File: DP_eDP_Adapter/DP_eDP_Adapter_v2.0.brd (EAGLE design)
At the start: 50 x 50 mm, 61 parts, among them IC1 AP6502A, IC2 tiny2313, IC3 TLC5947XLP

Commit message: 
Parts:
- moved C29 5.73 mm to (7.30, -4.32), flipped to the bottom
- moved C25 5.61 mm to (8.70, -4.32), flipped to the bottom
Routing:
- net LANE3_P: track 26.7 -> 0.00 mm, vias 2 -> 0
- net LANE3_N: track 26.7 -> 0.00 mm, vias 2 -> 0
- net HPD: track 36.2 -> 30.2 mm
- net N$19_N: track 6.67 -> 9.04 mm
- net N$19_P: track 6.70 -> 9.00 mm

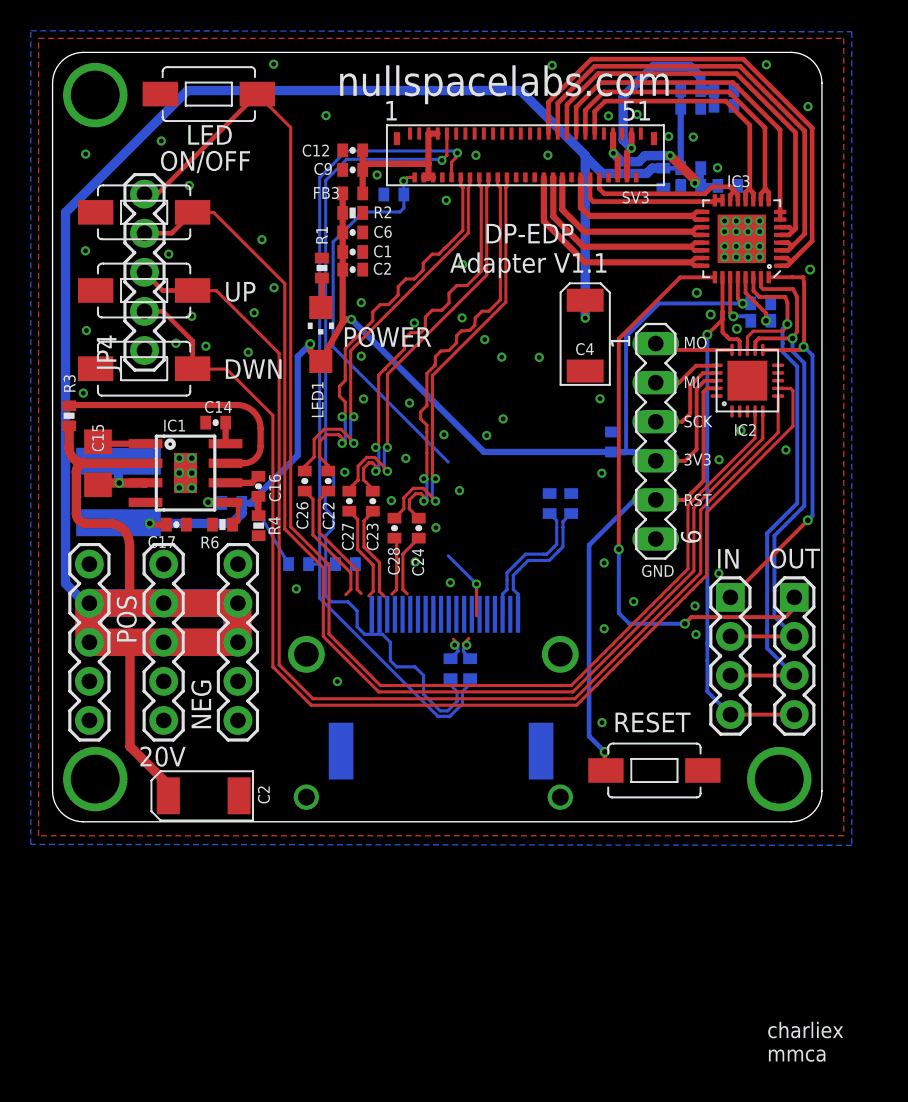
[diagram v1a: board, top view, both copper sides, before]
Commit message: 
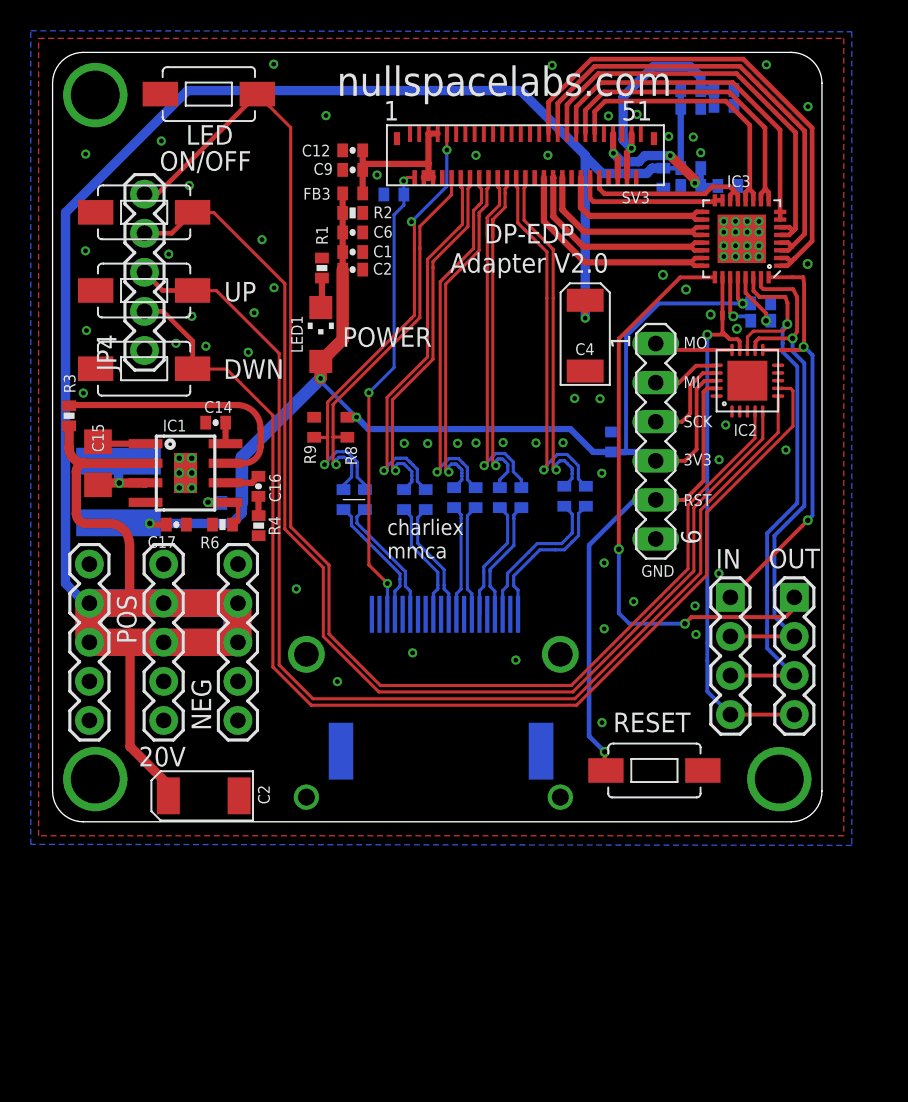
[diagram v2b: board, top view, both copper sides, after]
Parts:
- SV3: value DP_EDP_ADAPTER_EDP_CONNECTOR -> DP_EDP_ADAPTER_DP_EDP_ADAPTER_EDP_CONNECTOR; device DP_eDP_Adapter:DP_EDP_ADAPTER_EDP_MOLEX -> DP_eDP_Adapter_v2.0:DP_EDP_ADAPTER_DP_EDP_ADAPTER_EDP_MOLEX
- moved C20 13.7 mm to (-6.10, -4.06), turned to 270 degrees
- moved C21 12.3 mm to (-4.70, -4.06), turned to 270 degrees
- moved R8 9.44 mm to (-5.84, 0.64), flipped to the top, turned to 90 degrees
- moved R9 9.12 mm to (-8.00, 0.64), flipped to the top, turned to 270 degrees
- moved C28 7.13 mm to (4.06, -3.94), flipped to the bottom
- moved C24 6.96 mm to (5.46, -3.94), flipped to the bottom
- moved C27 6.81 mm to (1.09, -3.94), flipped to the bottom
- moved C23 6.68 mm to (2.49, -3.94), flipped to the bottom
- moved C26 6.56 mm to (-2.16, -4.06), flipped to the bottom
- moved C22 6.45 mm to (-0.75, -4.06), flipped to the bottom
- moved C29 1.06 mm to (8.26, -3.85)
- moved C25 1.06 mm to (9.65, -3.85)
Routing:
- net AUX_CH_N: track 54.3 -> 26.7 mm
- net LANE3_N: track 0.00 -> 24.7 mm, vias 0 -> 1
- net AUX_CH_P: track 54.3 -> 30.9 mm, vias 1 -> 3
- net LANE3_P: track 0.00 -> 23.4 mm, vias 0 -> 1
- net +3V3: track 93.3 -> 85.6 mm
- net AUX_P: track 2.05 -> 8.49 mm, vias 1 -> 0
- net AUX_N: track 2.09 -> 8.49 mm, vias 1 -> 0
- net LANE2_P: track 28.0 -> 23.8 mm, vias 2 -> 1
- net N$17_P: track 3.83 -> 7.90 mm
- net N$17_N: track 4.17 -> 7.90 mm
- net LANE1_P: track 27.0 -> 23.6 mm, vias 2 -> 1
- net LANE2_N: track 28.0 -> 25.1 mm, vias 2 -> 1
- net LANE1_N: track 27.0 -> 24.8 mm, vias 2 -> 1
- net LANE0_P: track 26.8 -> 24.7 mm, vias 2 -> 1
- net LANE0_N: track 26.9 -> 25.8 mm, vias 2 -> 1
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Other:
- board text added: "DP-EDP Adapter V2.0"
- board text removed: "DP-EDP Adapter V1.1"

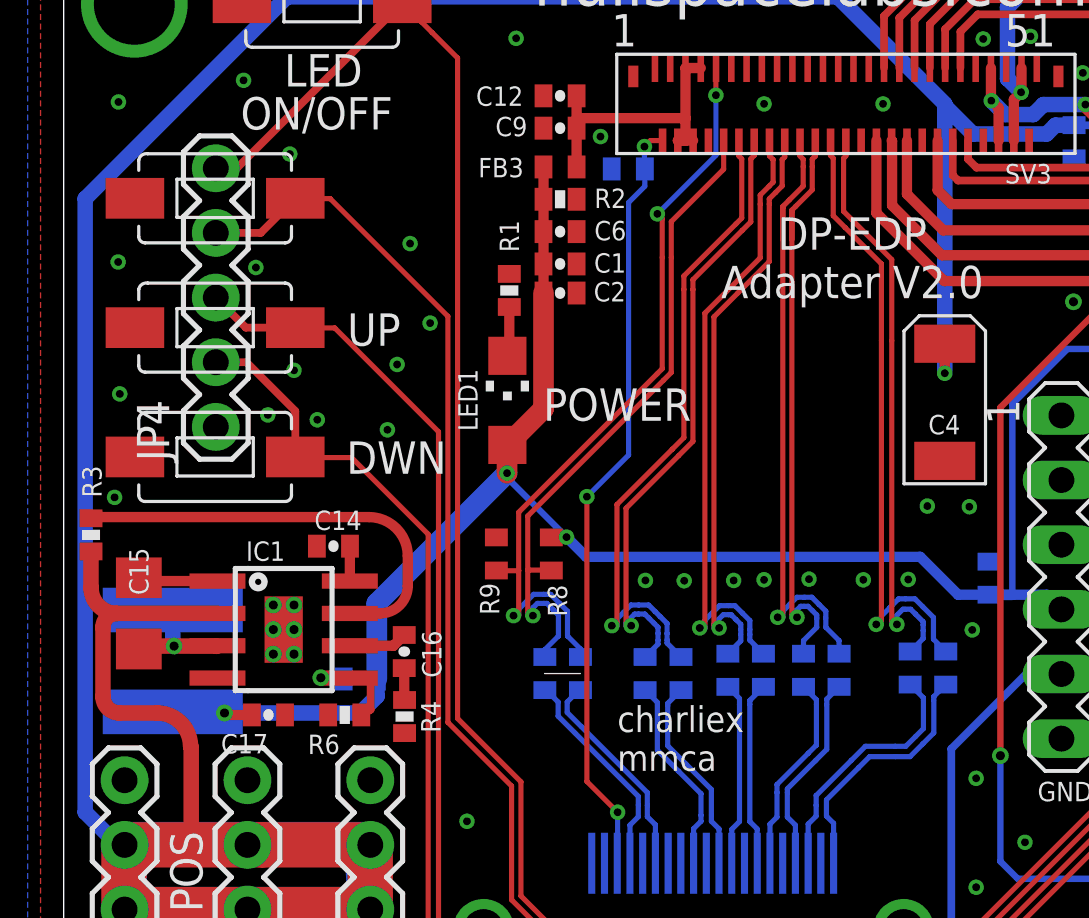
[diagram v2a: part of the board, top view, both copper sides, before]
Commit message: 
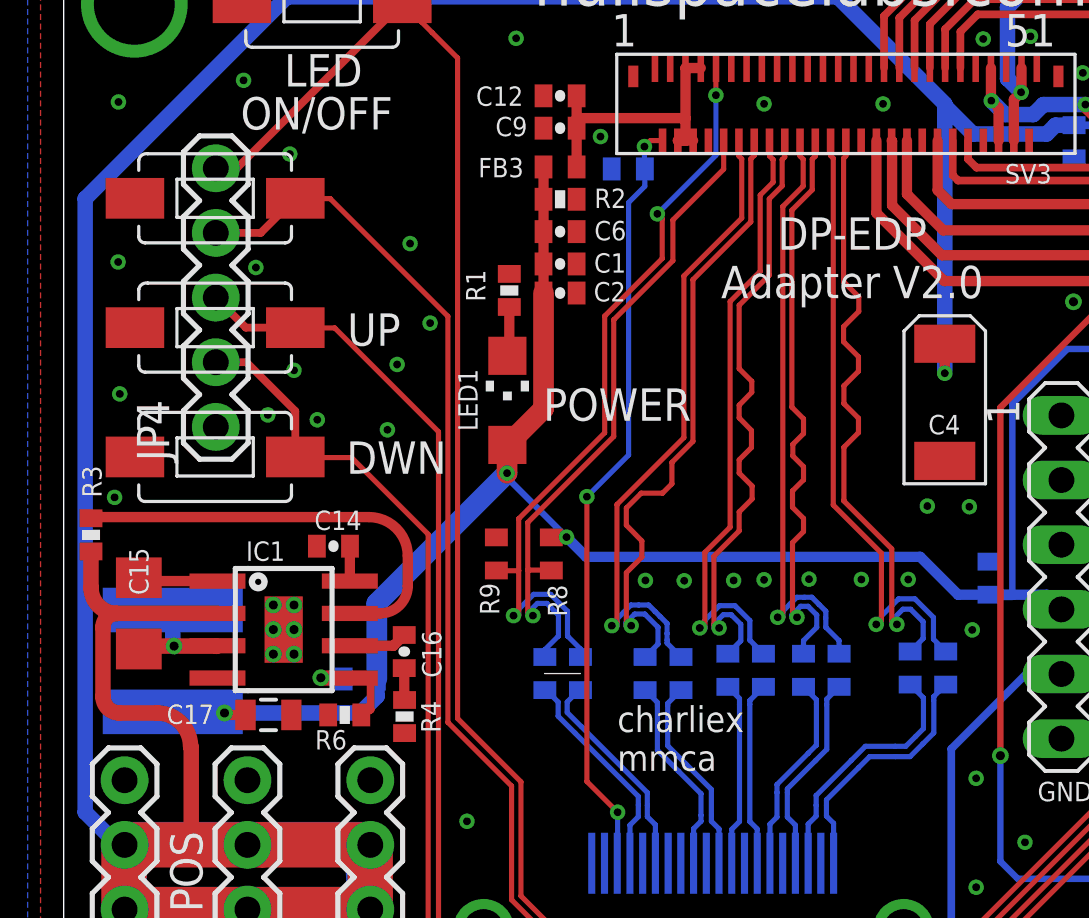
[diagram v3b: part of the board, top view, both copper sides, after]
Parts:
- C17: device SparkFun-Passives:0402-CAP -> SparkFun-Passives:0805
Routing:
- net LANE3_P: track 23.4 -> 24.8 mm
- net LANE2_N: track 25.1 -> 23.8 mm
- net LANE1_P: track 23.6 -> 24.8 mm
- net LANE0_P: track 24.7 -> 25.8 mm

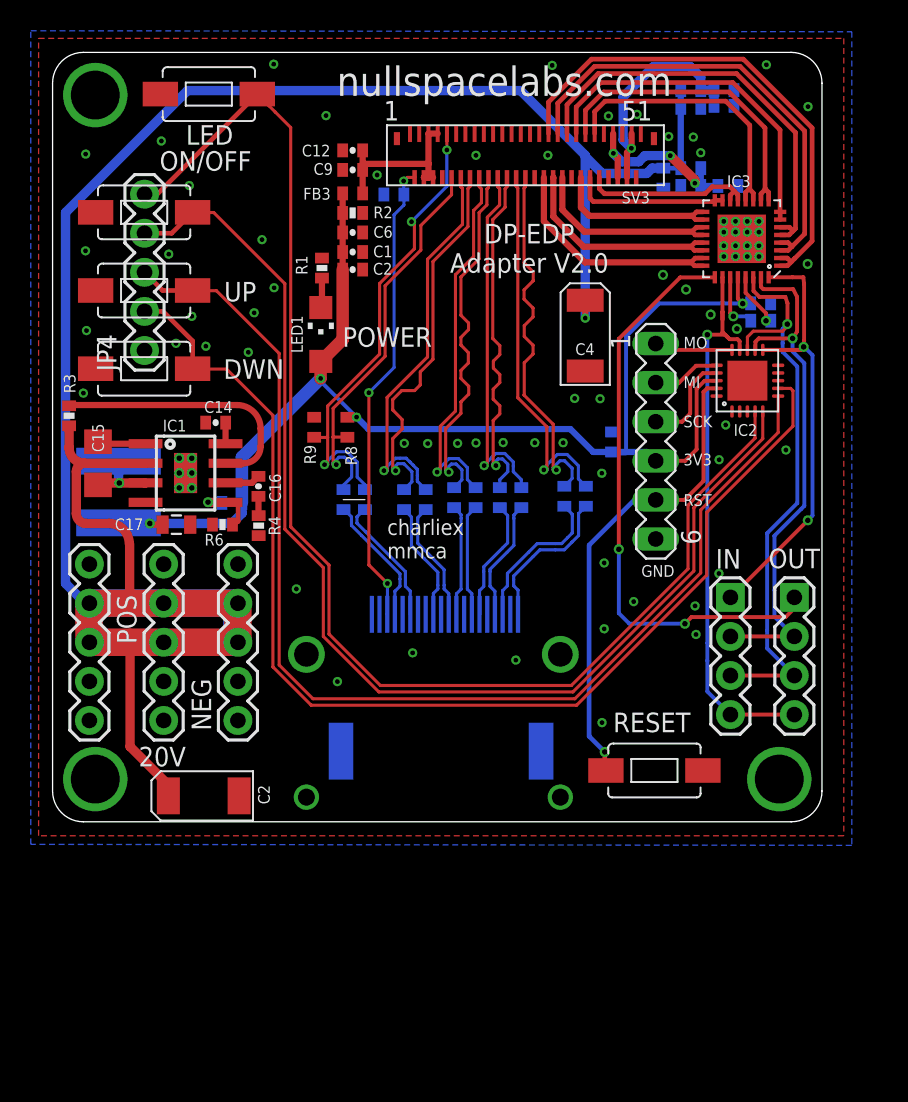
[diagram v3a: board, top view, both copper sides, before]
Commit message: 
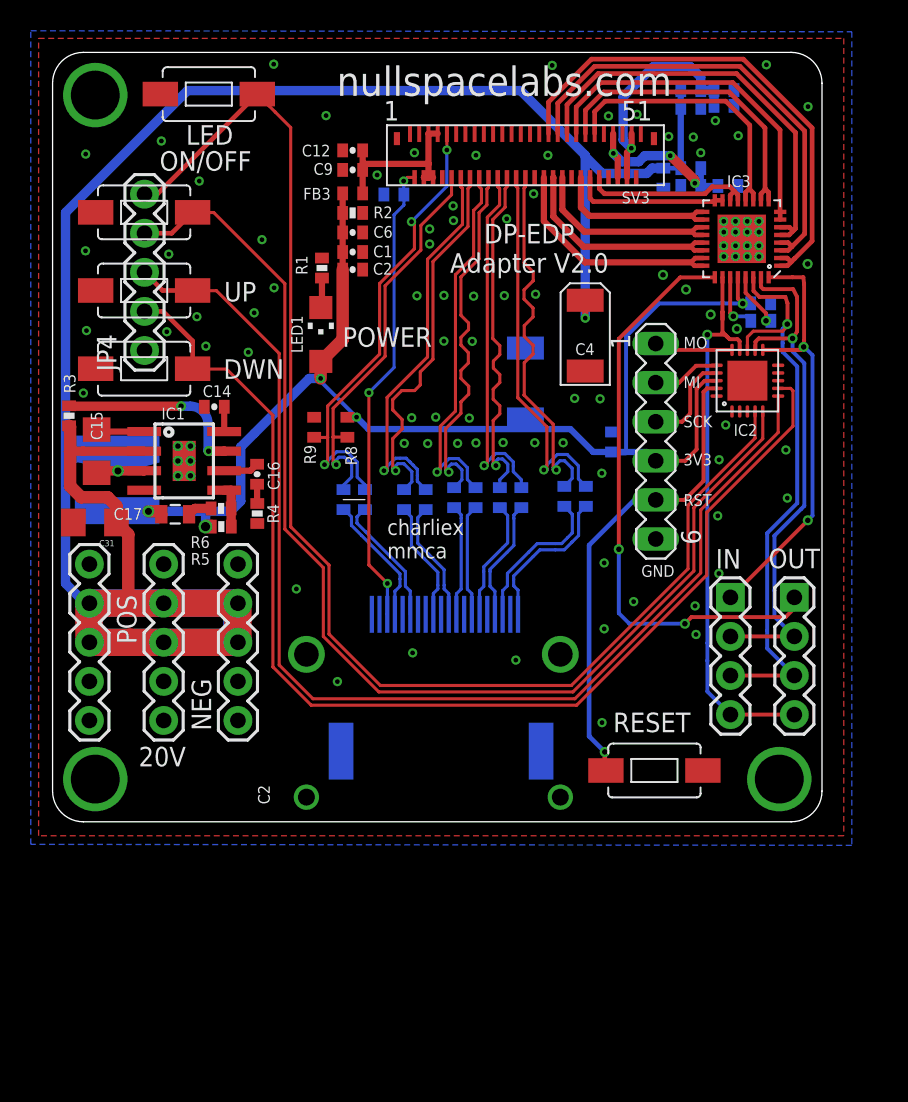
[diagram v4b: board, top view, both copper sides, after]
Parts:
- removed C13: 10uF 50V, SparkFun-Passives:EIA6032
- added C30: 100uF 50V, SparkFun-Passives:EIA6032
- added C31: 10uF 50V, SparkFun-Passives:1206
- moved R5 1.68 mm to (-14.0, -5.82), flipped to the top
- moved R6 1.06 mm to (-14.0, -4.64)
- moved C14 1.03 mm to (-14.5, 1.97)
- moved L4 0.79 mm to (-20.8, -2.78)
- moved C16 0.79 mm to (-11.7, -2.41)
- moved IC1 0.79 mm to (-16.4, -1.55)
- moved C15 0.79 mm to (-22.1, -0.91)
- moved R4 0.79 mm to (-11.7, -4.97)
- moved C17 0.68 mm to (-17.0, -5.02)
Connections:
- net +3V3: now also C30.P$1
- net 20V: now also C31.1; no longer C13.P$1
- net GND: now also C30.P$2, C31.2; no longer C13.P$2
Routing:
- net N$14: track 4.59 -> 16.5 mm
- net 20V: track 171.1 -> 160.7 mm
- net N$2: track 17.0 -> 12.3 mm, vias 0 -> 2
- net +3V3: track 85.4 -> 89.8 mm, vias 4 -> 5
- net GND: track 3.38 -> 4.97 mm, vias 79 -> 100
- net N$10: track 4.56 -> 3.63 mm, vias 1 -> 0
